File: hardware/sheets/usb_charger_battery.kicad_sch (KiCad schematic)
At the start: 43 parts, among them J301 USB-C receptacle (part TBD), J302 Battery JST-PH 2P, Q301 AO3400A, Q302 AO3400A, U301 TPD4E05U06, U302 BQ25620

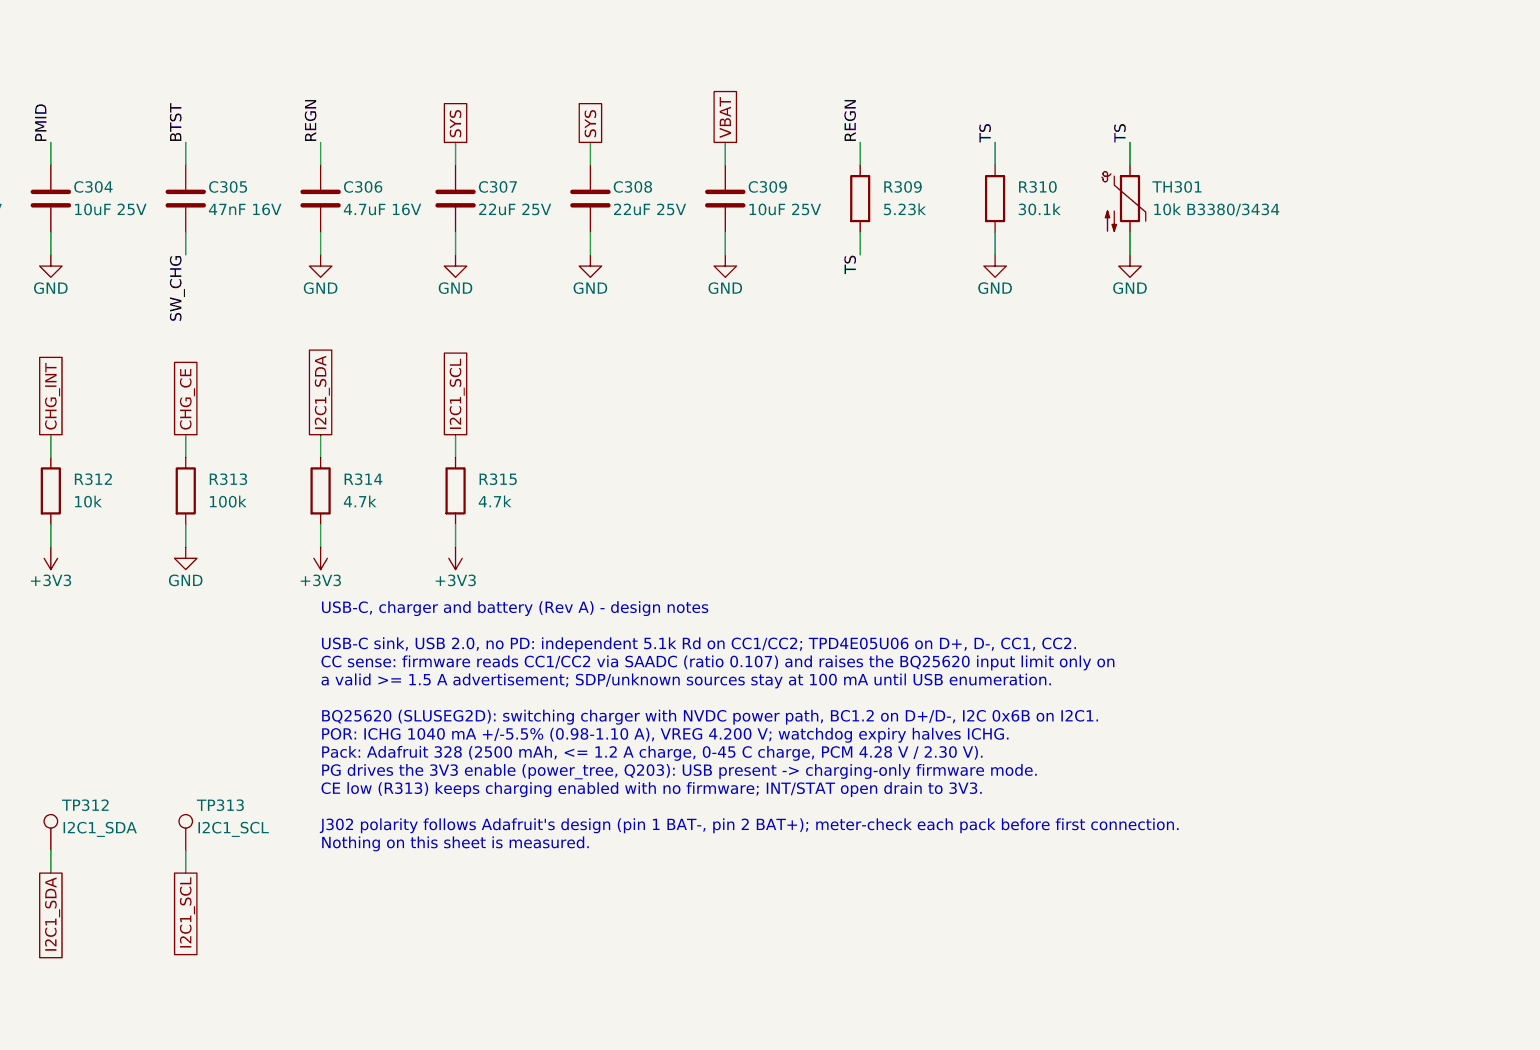
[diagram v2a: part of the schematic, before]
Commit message: hw: make the charger reset state safe for the pack
With TI's 5.23k/30.1k thermistor network, the BQ25620 reset JEITA
settings keep full charge current up to 60 C, past the pack's 45 C
charge limit. Use 10k from REGN with RT2 open: the reset comparators
then stop charging below about 0 C and above 41.7-44.5 C board
temperature in the worst case (comparator limits, 1% resistor, NTC
R25 and B tolerance), with no firmware involved. The RT2 footprint
stays as an option.

Pull CE up to 3V3 instead of down, so the charger does not charge
until firmware has set the input limit and temperature thresholds,
and an MCU reset stops charging. Until then the USB input carries
only the logic load.
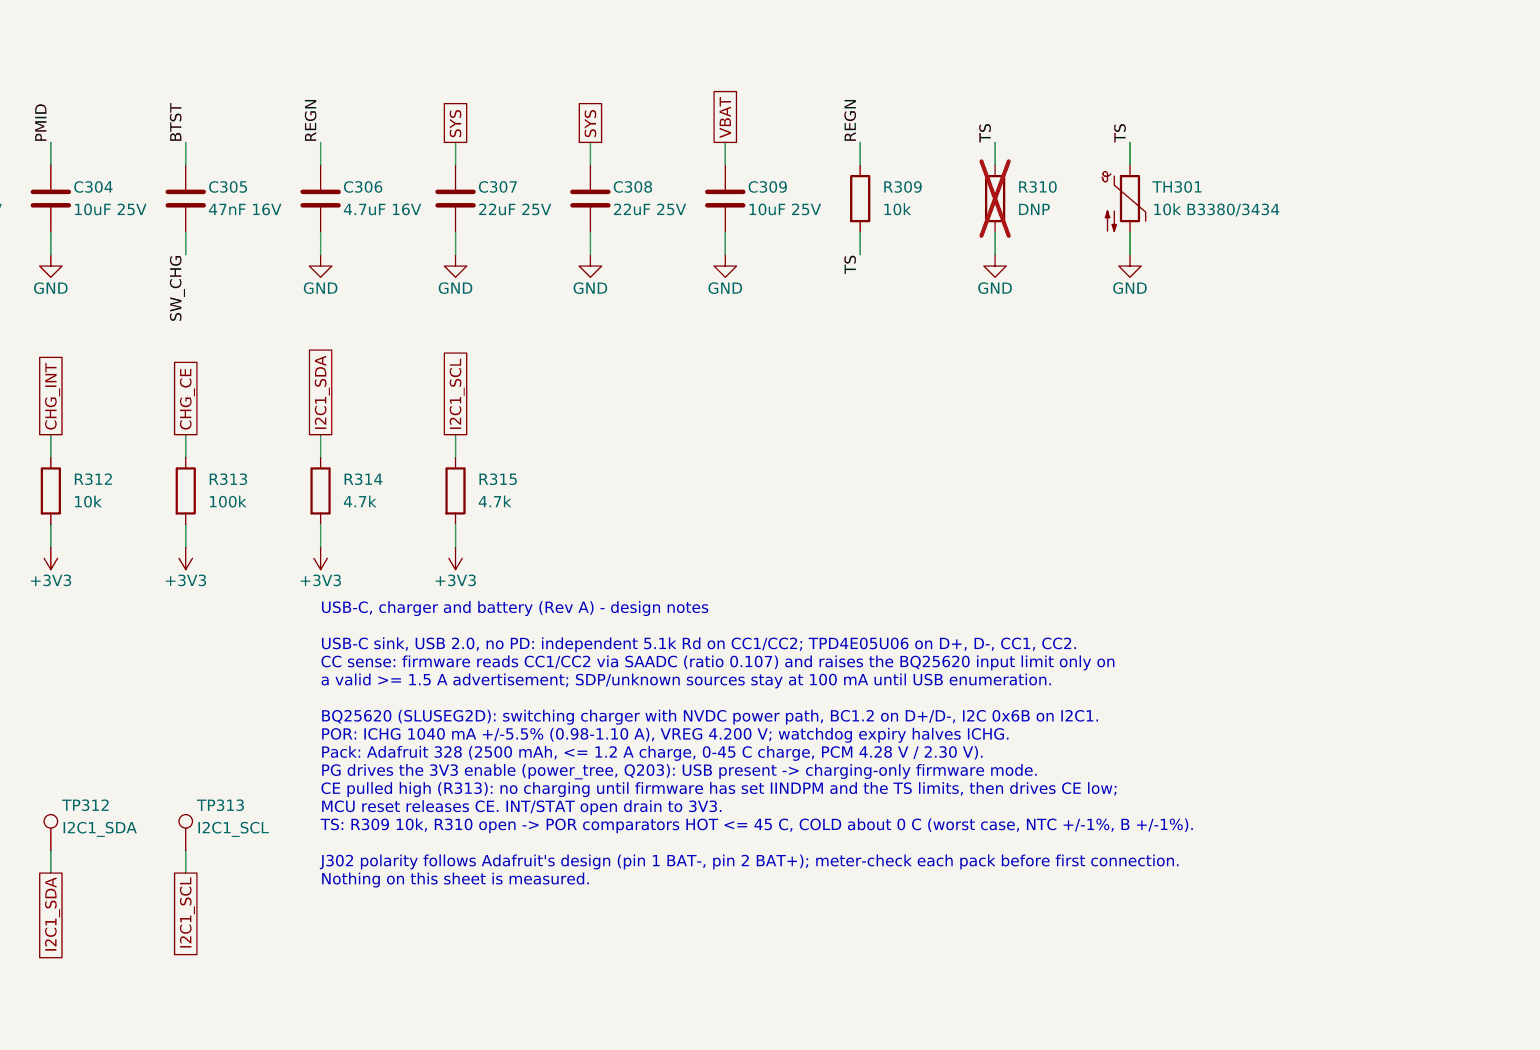
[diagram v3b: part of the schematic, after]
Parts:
- R309: value 5.23k -> 10k; LCSC C25907 -> C25744; MPN 0402WGF5231TCE -> 0402WGF1002TCE; Note RT1 (SLUSEG2D 8.3.5.4.2) -> RT1: with R310 open, default HOT <= 45 C and COLD about 0 C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
- R310: value 30.1k -> DNP; LCSC C29402 -> (none); MPN 0402WGF3012TCE -> (none); Manufacturer UNI-ROYAL(Uniroyal Elec) -> (none); Note RT2 -> RT2 position, open: fitting 30.1k restores TI's 0-60 C netw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; now not fitted
- R313: Note CE low: charging enabled without firmware; MCU drives high 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 -> CE high: charging off until firmware configures the charger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
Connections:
- net +3V3: now also R313.2
- net GND: no longer R313.2
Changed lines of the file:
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@@
 			)
 		)
-		(property "Value" "5.23k"
+		(property "Value" "10k"
 			(at 292.1 133.35 0)
 			(effects
@@
 			)
 		)
-		(property "MPN" "0402WGF5231TCE"
+		(property "MPN" "0402WGF1002TCE"
 			(at 289.56 132.08 0)
 			(hide yes)
@@
 			)
 		)
-		(property "LCSC" "C25907"
+		(property "LCSC" "C25744"
 			(at 289.56 132.08 0)
 			(hide yes)
@@
 			)
 		)
-		(property "Note" "RT1 (SLUSEG2D 8.3.5.4.2)"
+		(property "Note" "RT1: with R310 open, default HOT <= 45 C and COLD about 0 C worst case"
 			(at 289.56 132.08 0)
 			(hide yes)
@@
 		(in_bom yes)
 		(on_board yes)
-		(dnp no)
+		(dnp yes)
 		(property "Reference" "R310"
 			(at 307.34 130.81 0)
@@
 			)
 		)
-		(property "Value" "30.1k"
+		(property "Value" "DNP"
 			(at 307.34 133.35 0)
 			(effects
@@
 			)
 		)
-		(property "Manufacturer" "UNI-ROYAL(Uniroyal Elec)"
-			(at 304.8 132.08 0)
-			(hide yes)
-			(effects
-				(font
-					(size 1.27 1.27)
-				)
-			)
-		)
-		(property "MPN" "0402WGF3012TCE"
-			(at 304.8 132.08 0)
-			(hide yes)
-			(effects
-				(font
-					(size 1.27 1.27)
-				)
-			)
-		)
-		(property "LCSC" "C29402"
-			(at 304.8 132.08 0)
-			(hide yes)
-			(effects
-				(font
-					(size 1.27 1.27)
-				)
-			)
-		)
-		(property "Note" "RT2"
+		(property "Note" "RT2 position, open: fitting 30.1k restores TI's 0-60 C network"
 			(at 304.8 132.08 0)
 			(hide yes)
@@
 			)
 		)
-		(property "Note" "CE low: charging enabled without firmware; MCU drives high to pause"
+		(property "Note" "CE high: charging off until firmware configures the charger and drives CE low"
 			(at 213.36 165.1 0)
 			(hide yes)
@@
 	)
 	(symbol
-		(lib_id "power:GND")
-		(at 213.36 171.45 0)
+		(lib_id "power:+3V3")
+		(at 213.36 171.45 180)
 		(unit 1)
 		(exclude_from_sim no)
@@
 			)
 		)
-		(property "Value" "GND"
+		(property "Value" "+3V3"
 			(at 213.36 175.26 0)
 			(effects
@@
 			)
 		)
-		(property "Description" "Power symbol creates a global label with name \"GND\" , ground"
+		(property "Description" "Power symbol creates a global label with name \"+3V3\""
 			(at 213.36 171.45 0)
 			(hide yes)
@@
 		)
 	)
-	(text "USB-C, charger and battery (Rev A) - design notes\n\nUSB-C sink, USB 2.0, no PD: independent 5.1k Rd on CC1/CC2; TPD4E05U06 on D+, D-, CC1, CC2.\nCC sense: firmware reads CC1/CC2 via SAADC (ratio 0.107) and raises the BQ25620 input limit only on\na valid >= 1.5 A advertisement; SDP/unknown sources stay at 100 mA until USB enumeration.\n\nBQ25620 (SLUSEG2D): switching charger with NVDC power path, BC1.2 on D+/D-, I2C 0x6B on I2C1.\nPOR: ICHG 1040 mA +/-5.5% (0.98-1.10 A), VREG 4.200 V; watchdog expiry halves ICHG.\nPack: Adafruit 328 (2500 mAh, <= 1.2 A charge, 0-45 C charge, PCM 4.28 V / 2.30 V).\nPG drives the 3V3 enable (power_tree, Q203): USB present -> charging-only firmware mode.\nCE low (R313) keeps charging enabled with no firmware; INT/STAT open drain to 3V3.\n\nJ302 polarity follows Adafruit's design (pin 1 BAT-, pin 2 BAT+); meter-check each pack before first connection.\nNothing on this sheet is measured."
+	(text "USB-C, charger and battery (Rev A) - design notes\n\nUSB-C sink, USB 2.0, no PD: independent 5.1k Rd on CC1/CC2; TPD4E05U06 on D+, D-, CC1, CC2.\nCC sense: firmware reads CC1/CC2 via SAADC (ratio 0.107) and raises the BQ25620 input limit only on\na valid >= 1.5 A advertisement; SDP/unknown sources stay at 100 mA until USB enumeration.\n\nBQ25620 (SLUSEG2D): switching charger with NVDC power path, BC1.2 on D+/D-, I2C 0x6B on I2C1.\nPOR: ICHG 1040 mA +/-5.5% (0.98-1.10 A), VREG 4.200 V; watchdog expiry halves ICHG.\nPack: Adafruit 328 (2500 mAh, <= 1.2 A charge, 0-45 C charge, PCM 4.28 V / 2.30 V).\nPG drives the 3V3 enable (power_tree, Q203): USB present -> charging-only firmware mode.\nCE pulled high (R313): no charging until firmware has set IINDPM and the TS limits, then drives CE low;\nMCU reset releases CE. INT/STAT open drain to 3V3.\nTS: R309 10k, R310 open -> POR comparators HOT <= 45 C, COLD about 0 C (worst case, NTC +/-1%, B +/-1%).\n\nJ302 polarity follows Adafruit's design (pin 1 BAT-, pin 2 BAT+); meter-check each pack before first connection.\nNothing on this sheet is measured."
 		(exclude_from_sim no)
 		(at 228.6 177.8 0)

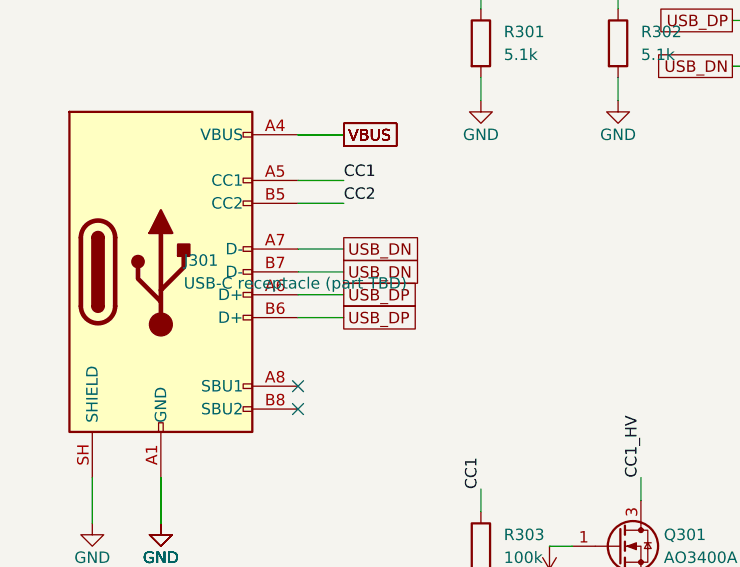
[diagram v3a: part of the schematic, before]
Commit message: hw: select USB-C receptacle and power switch
Use the HRO TYPE-C-31-M-12 receptacle and the C&K PCM12SMTR right-angle
slide switch. KiCad's footprints for both match the vendor drawings,
and the switch's common terminal is on SYS as drawn.
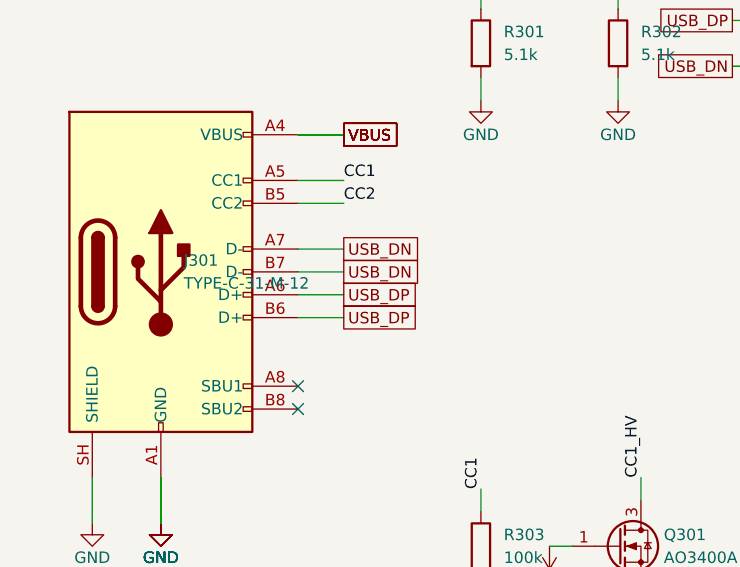
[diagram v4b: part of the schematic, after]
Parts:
- J301: value USB-C receptacle (part TBD) -> TYPE-C-31-M-12; footprint (none) -> Connector_USB:USB_C_Receptacle_HRO_TYPE-C-31-M-12; LCSC (none) -> C165948; MPN (none) -> TYPE-C-31-M-12; Manufacturer (none) -> Korean Hroparts Elec; Note Mechanical gate: receptacle MPN/footprint not selected (can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 -> 16-pin USB 2.0 receptacle, bottom edge, rear side; footprin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
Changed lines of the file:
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@@
 			)
 		)
-		(property "Value" "USB-C receptacle (part TBD)"
+		(property "Value" "TYPE-C-31-M-12"
 			(at 35.56 77.47 0)
 			(effects
@@
 			)
 		)
-		(property "Footprint" ""
+		(property "Footprint" "Connector_USB:USB_C_Receptacle_HRO_TYPE-C-31-M-12"
 			(at 33.02 76.2 0)
 			(hide yes)
@@
 			)
 		)
-		(property "Note" "Mechanical gate: receptacle MPN/footprint not selected (candidate TYPE-C-31-M-12)"
+		(property "Manufacturer" "Korean Hroparts Elec"
 			(at 33.02 76.2 0)
 			(hide yes)
+			(effects
+				(font
+					(size 1.27 1.27)
+				)
+			)
+		)
+		(property "MPN" "TYPE-C-31-M-12"
+			(at 33.02 76.2 0)
+			(hide yes)
+			(effects
+				(font
+					(size 1.27 1.27)
+				)
+			)
+		)
+		(property "LCSC" "C165948"
+			(at 33.02 76.2 0)
+			(hide yes)
+			(effects
+				(font
+					(size 1.27 1.27)
+				)
+			)
+		)
+		(property "Note" "16-pin USB 2.0 receptacle, bottom edge, rear side; footprint checked against the HRO drawing (2020-12-08)"
+			(at 33.02 76.2 0)
+			(hide yes)

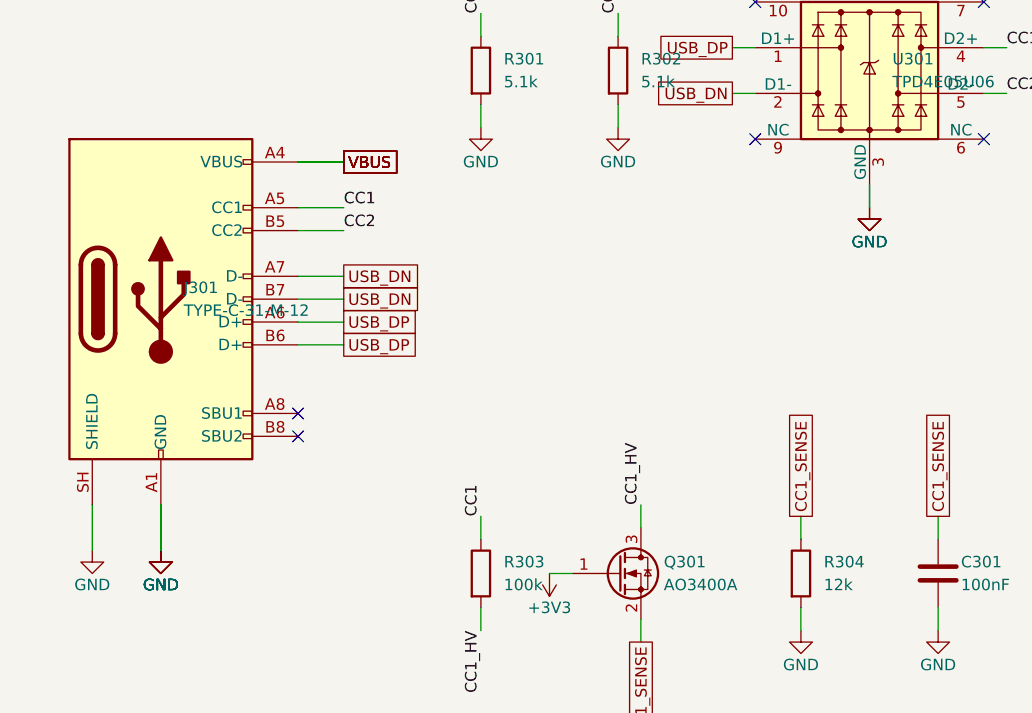
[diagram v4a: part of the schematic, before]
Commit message: hw: draw LED matrix, row and column drivers and scan-stall safety (#8)
* repo: ignore KiCad local history

KiCad 10 keeps automatic snapshots in a .history folder (with its own
Git repository) next to the project. Ignore it, and make the hygiene
check reject it, so local history cannot be committed.

* hw: save schematic sheets in KiCad's own format

Opening and saving the project in KiCad 10 rewrites the generated
sheets and project file in its native layout. KiCad also merges seven
overlapping wire segments on the USB sheet. Nets, values and
footprints are unchanged, so committing this once keeps later edits
made in KiCad free of formatting churn.

* hw: add column driver and monostable symbols

Add a TLC59283 symbol with the RGE (VQFN-24) pin numbers from TI's pin
table; it uses KiCad's footprint for TI's RGE0024C package. Add a
single-unit SN74LVC1G123 symbol, because KiCad's version keeps the
supply pins in a separate unit.

* hw: draw matrix driver and LED matrix sheets

Columns: two cascaded TLC59283 sinks on 3V3. R_IREF is 2.94k, an
18.0 mA nominal setting (about 19.4 mA worst case with driver and
resistor tolerance), with a fitted 0 ohm in series, so adjustment can
only lower the current.

Rows: the TLC chain output, clock, latch and SAFE cross into the LED
rail through an SN74LVC8T245 translator. Four SN74HC595 on VLED drive
32 AO3401A high-side switches with 10k gate pull-ups, with row
pull-downs as unfitted options.

Scan-stall safety: every latch retriggers an SN74LVC1G123. TI
specifies 1.0-1.1 ms at 10k / 0.1 uF; with the fitted parts'
tolerances the timeout is 0.76-1.41 ms. The part has only a Q
output, so an inverter makes SAFE = NOT Q. SAFE forces the column
BLANK through an OR gate and tri-states the row registers, and the
MCU reads it. The matrix stays dark while the MCU is off or in
reset.

LED matrix: 1024 LEDs, anodes on the rows and cathodes on the
columns, drawn as row and column buses, on the front side with the
buttons (ADR 0008).

The pend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
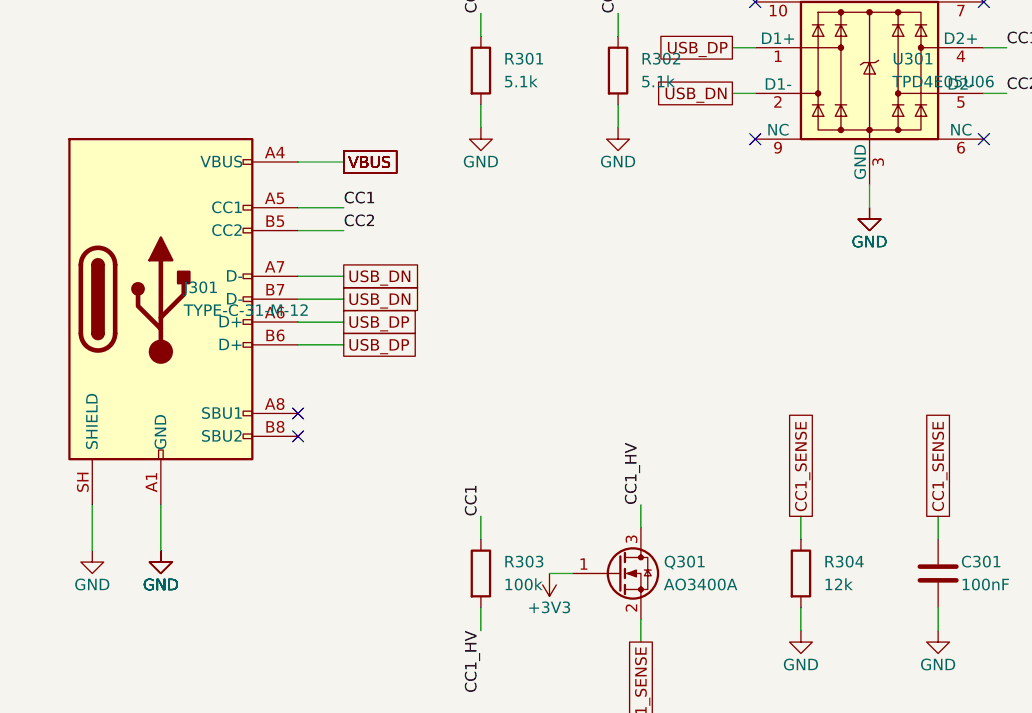
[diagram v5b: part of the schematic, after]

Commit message: hw: use TI's DQA0010A land pattern for the USB ESD array
KiCad's generic USON-10 footprint comes from another TI part and has
0.30 mm pads on all ten pins with the rows 0.77 mm apart. TI's
DQA0010A land pattern for the TPD4E05U06 uses 0.20 mm signal pads,
0.40 mm ground pads (pins 3 and 8) and rows 0.835 mm apart, with
narrower paste on the ground pads. The new project footprint follows
TI's land pattern and stencil examples.

TI also lists a DQA0010B outline whose pins 3 and 8 are joined by
exposed metal, so no other net may pass between those pads.
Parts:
- U301: footprint Package_SON:USON-10_2.5x1.0mm_P0.5mm -> smart-led-badge:TI_DQA0010A_USON-10_2.5x1.0mm_P0.5mm
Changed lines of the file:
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@@
 			)
 		)
-		(property "Footprint" "Package_SON:USON-10_2.5x1.0mm_P0.5mm"
+		(property "Footprint" "smart-led-badge:TI_DQA0010A_USON-10_2.5x1.0mm_P0.5mm"
 			(at 111.76 50.8 0)
 			(hide yes)
